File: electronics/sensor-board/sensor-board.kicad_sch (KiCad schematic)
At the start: 32 parts

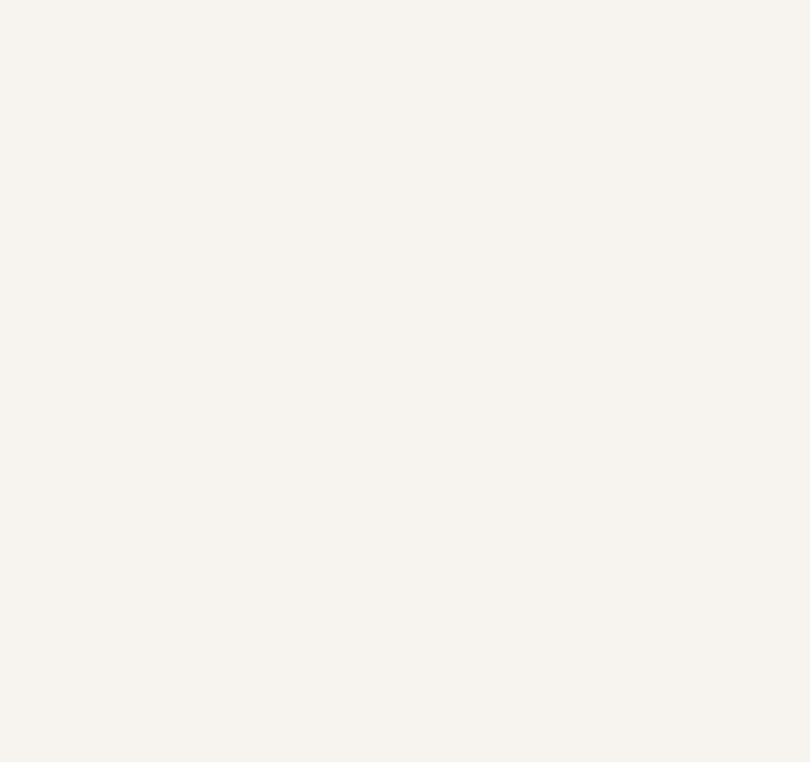
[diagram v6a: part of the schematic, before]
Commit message: Added Op Amp Library to sensor-board
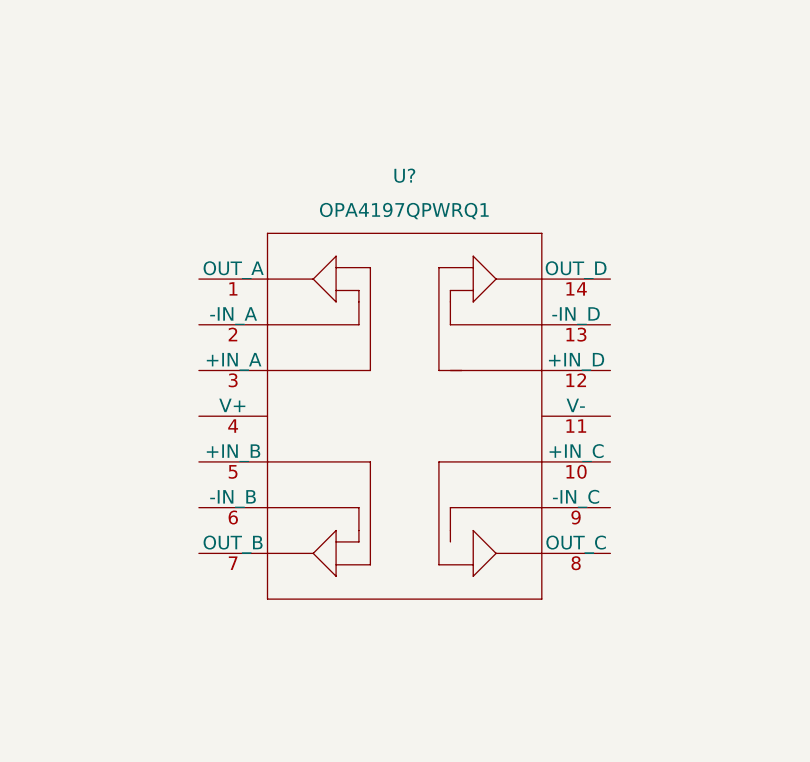
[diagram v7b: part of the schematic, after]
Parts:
- added U?: OPA4197QPWRQ1, TSSOP_QPWRQ1_TEX, symbol OPA4197QPWRQ1:OPA4197QPWRQ1
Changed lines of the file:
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@@
     (pin "8")
+  )
+  (symbol (lib_id "OPA4197QPWRQ1:OPA4197QPWRQ1") (at 87.63 172.72 0) (unit 1)
+    (in_bom yes) (on_board yes) (fields_autoplaced)
+    (property "Reference" "U?" (id 0) (at 110.49 161.29 0)
+      (effects (font (size 1.524 1.524)))
+    )
+    (property "Value" "OPA4197QPWRQ1" (id 1) (at 110.49 165.1 0)
+      (effects (font (size 1.524 1.524)))
+    )
+    (property "Footprint" "TSSOP_QPWRQ1_TEX" (id 2) (at 110.49 161.544 0)
+      (effects (font (size 1.524 1.524)) hide)
+    )
+    (property "Datasheet" "" (id 3) (at 87.63 172.72 0)
+      (effects (font (size 1.524 1.524)))
+    )
+    (pin "1")
+    (pin "10")
+    (pin "11")
+    (pin "12")
+    (pin "13")
+    (pin "14")
+    (pin "2")
+    (pin "3")
+    (pin "4")
+    (pin "5")
+    (pin "6")
+    (pin "7")
+    (pin "8")
+    (pin "9")
   )
   (symbol (lib_id "MCU_ST_STM32F4:STM32F446ZEHx") (at 252.73 158.75 0) (unit 1)
@@
       (reference "U?") (unit 1) (value "MAX33012EASA+") (footprint "21-0041-3-M_90-0096-8L_MXM")
     )
+    (path "/864bedde-edbe-47fd-be9e-9a9d9c5cefa4"
+      (reference "U?") (unit 1) (value "OPA4197QPWRQ1") (footprint "TSSOP_QPWRQ1_TEX")
+    )
     (path "/d6bb79fa-0858-4930-b37d-d4cacdd21cc4"

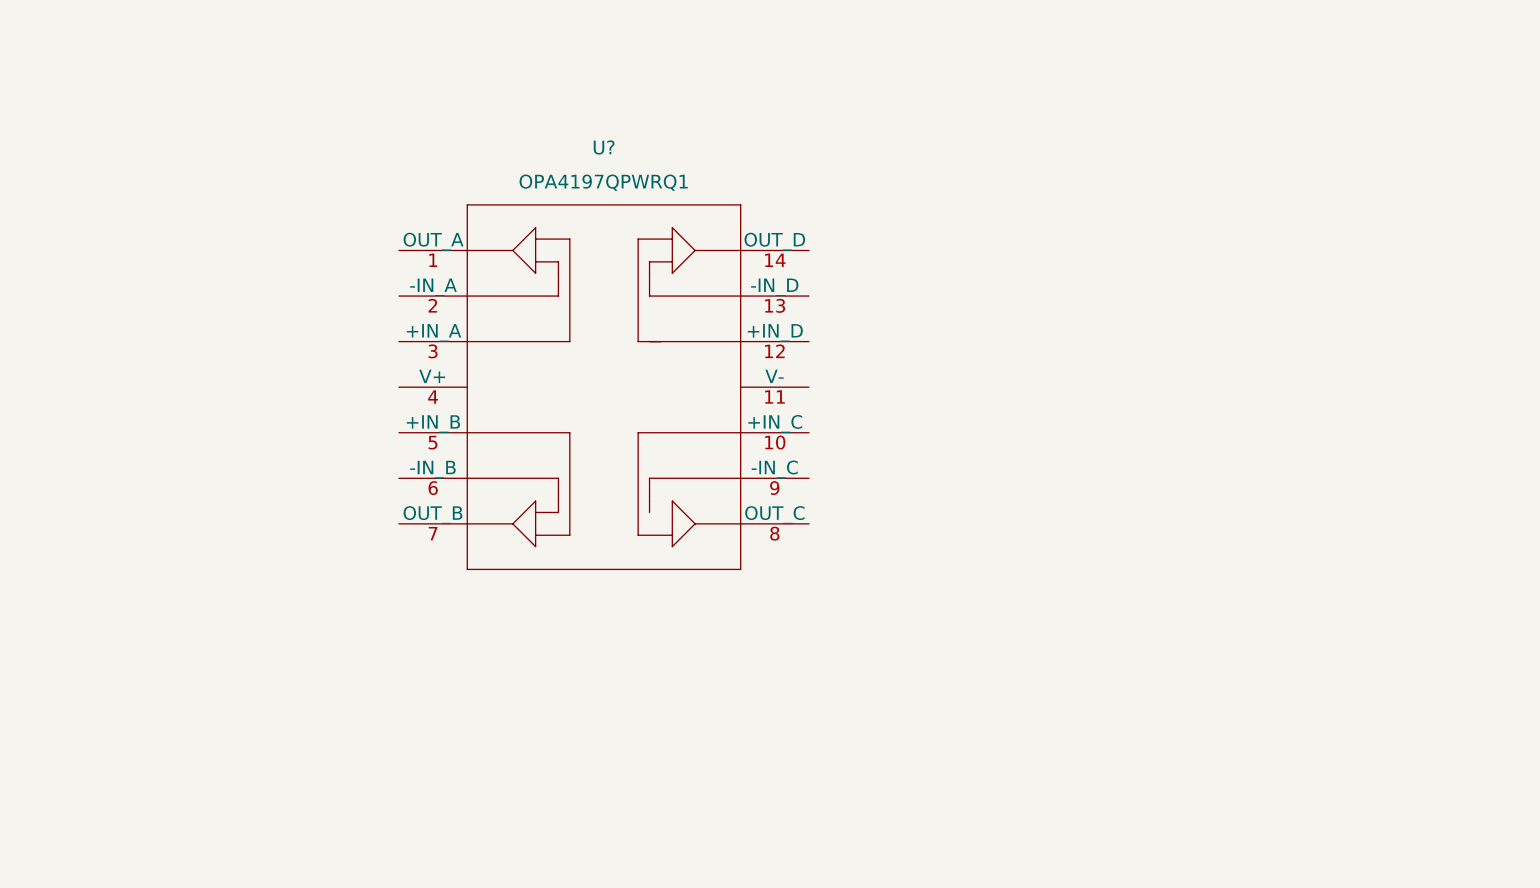
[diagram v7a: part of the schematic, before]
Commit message: added datasheet, modified sensor-board schematic
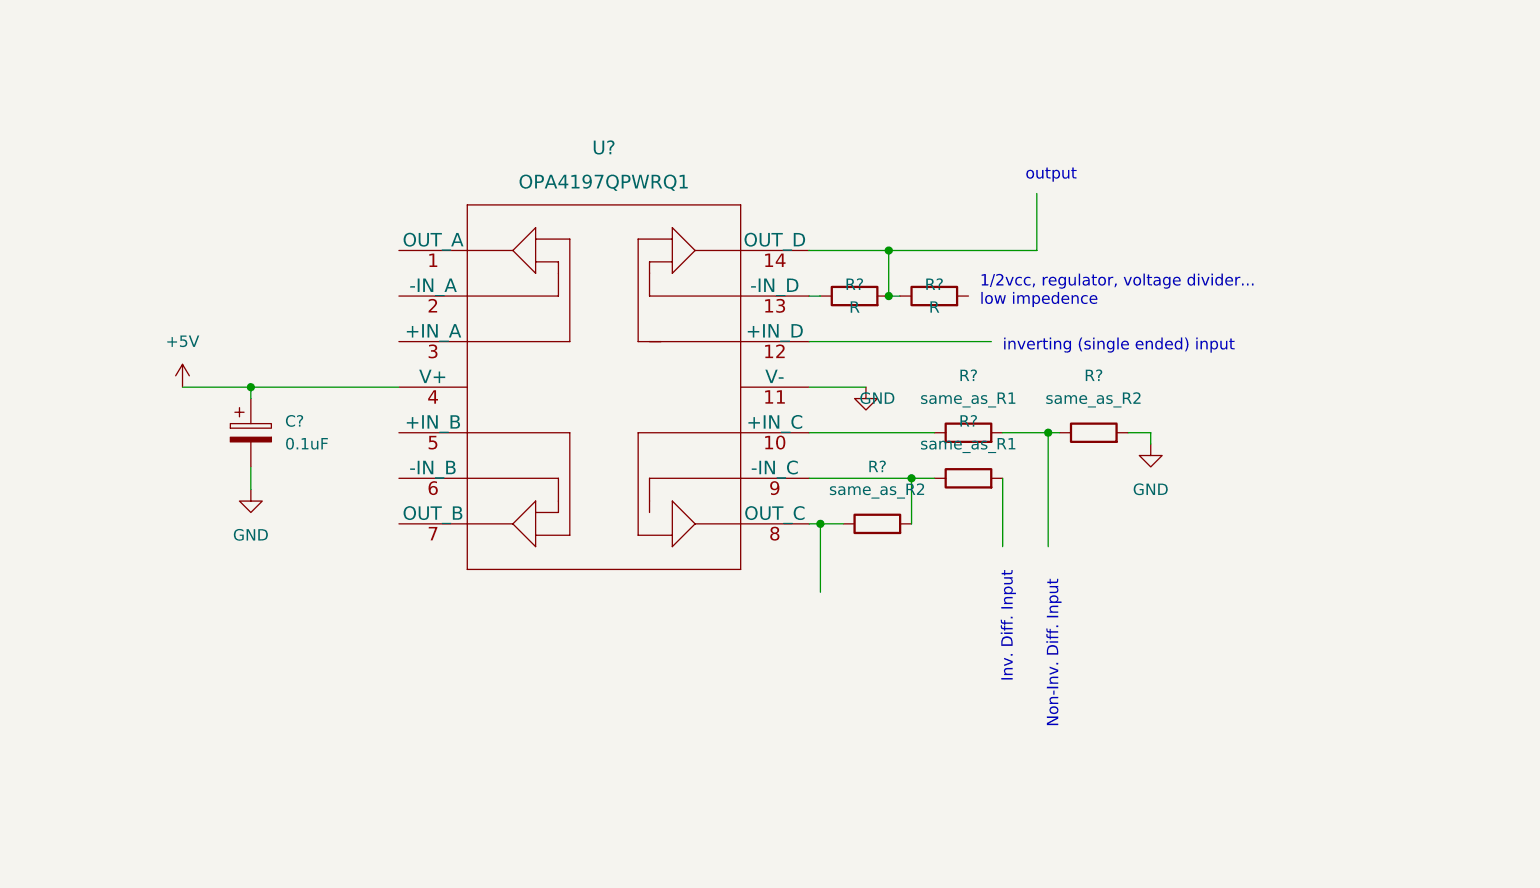
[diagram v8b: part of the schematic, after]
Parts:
- added C?: 0.1uF, symbol Device:C_Polarized
- added R? (x2): R, symbol Device:R
- added R? (x2): same_as_R1, symbol Device:R
- added R? (x2): same_as_R2, symbol Device:R
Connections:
- net +5V: now also U?.4 (V+), C?.1
- net GND: now also U?.11 (V-), C?.2, R?.2
- net at U?.10 (+IN_C): now also R?.1
- net at U?.13 (-IN_D): now also R?.1
- net at U?.14 (OUT_D): now also R?.1, R?.2
- net at U?.8 (OUT_C): now also R?.1
- net at U?.9 (-IN_C): now also R?.1, R?.2
- new net: R?.1, R?.2
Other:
- note added: "1/2vcc, regulator, voltage divider... low impedence"
- note added: "Inv. Diff. Input"
- note added: "Non-Inv. Diff. Input"
- note added: "inverting (single ended) input"
- note added: "output"
